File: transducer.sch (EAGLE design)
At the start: 12 parts, among them U1 ADS1014IDGST

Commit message: Transducer board routed.
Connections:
- net N$3 renamed ADR
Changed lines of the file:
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@@
 </segment>
 </net>
-<net name="N$3" class="0">
+<net name="ADR" class="0">
 <segment>
 <pinref part="U1" gate="A" pin="ADDR"/>

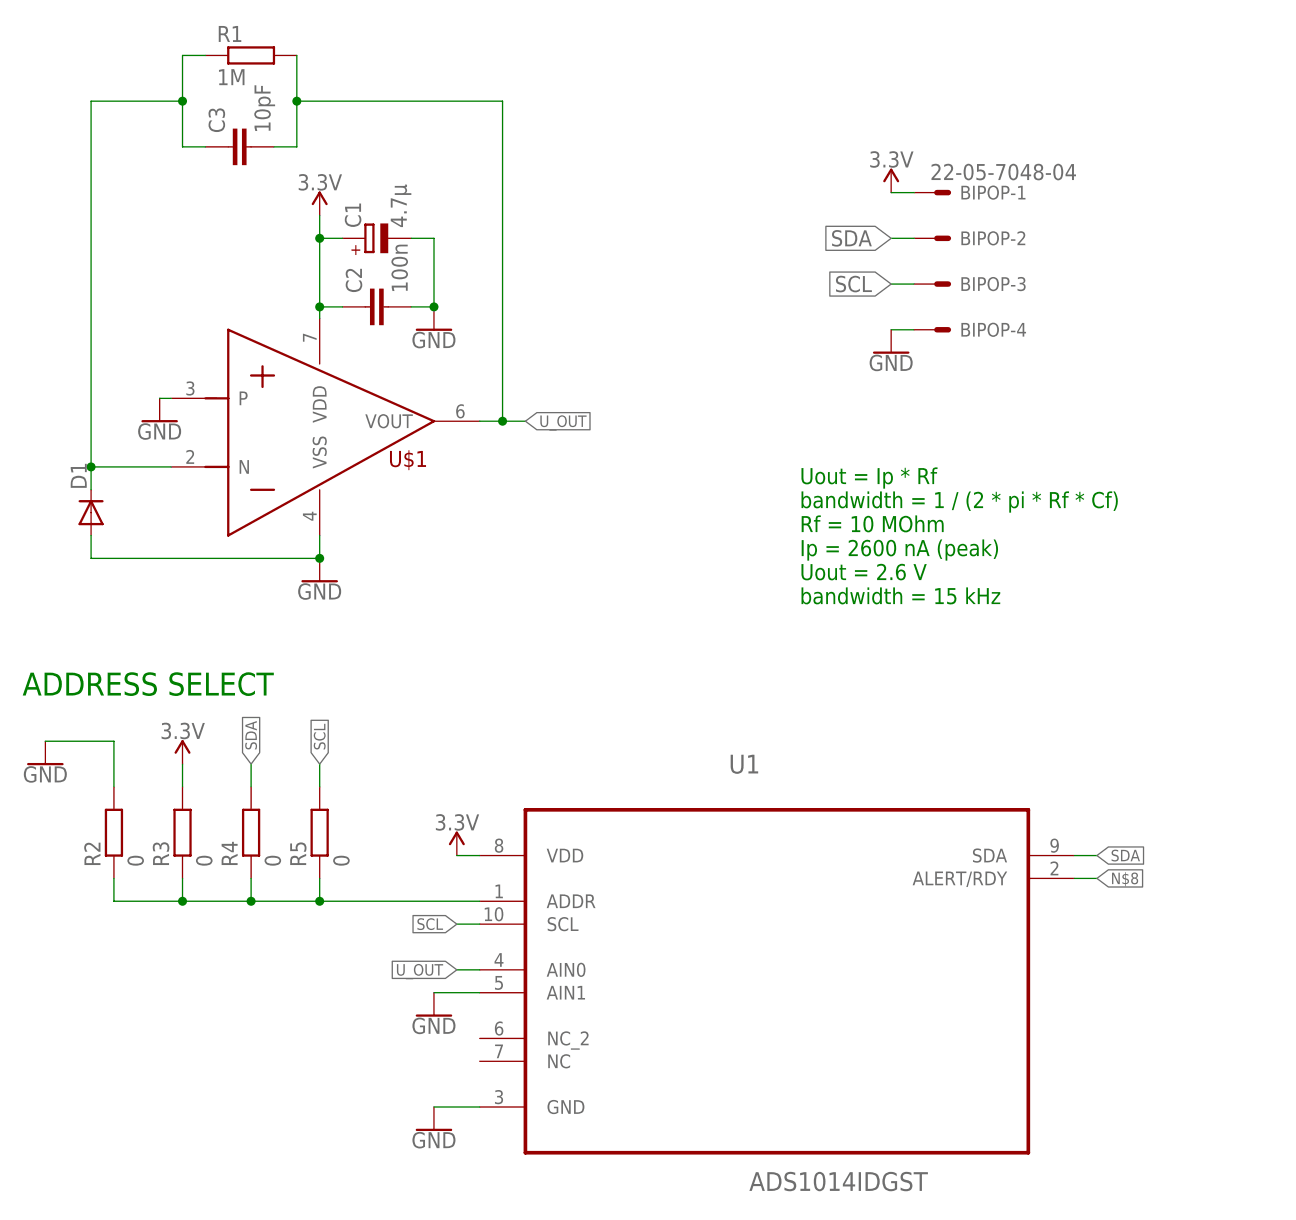
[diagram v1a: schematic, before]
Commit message: UV transducer board redesigned according to SGlux tips
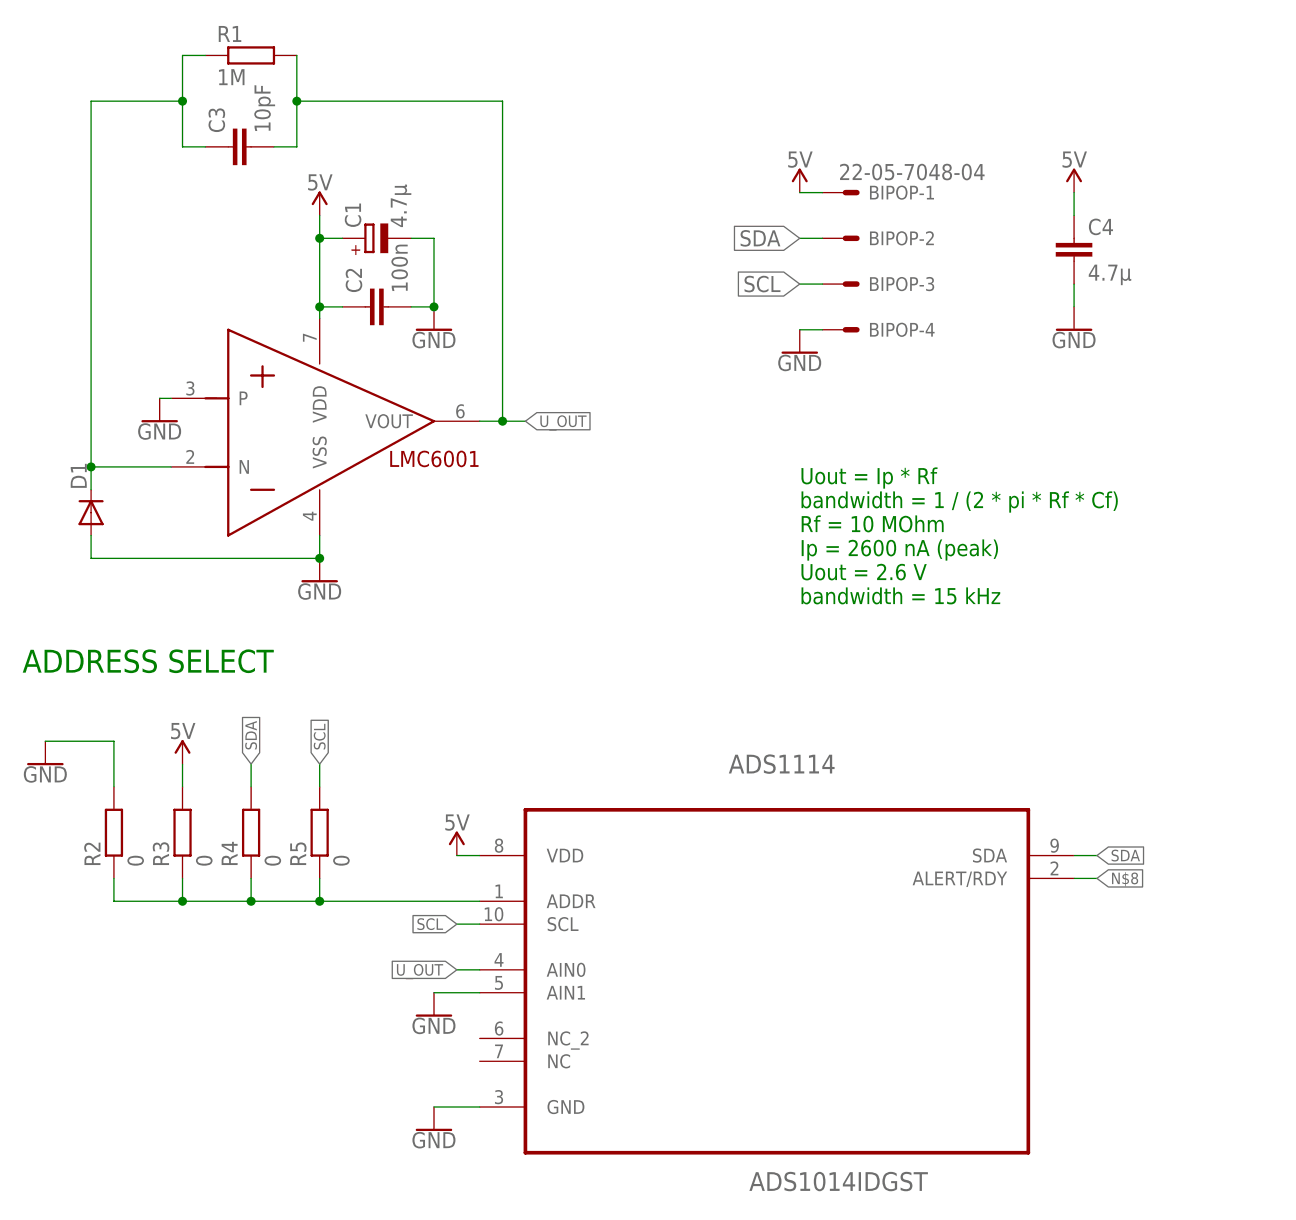
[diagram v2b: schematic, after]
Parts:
- added C4: 4.7µ, rcl:C-EUC0805
- renumbered U$1 to LMC6001, U1 to ADS1114
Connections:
- net N$5 renamed CATH
- removed net 3.3V: ADS1114.VDD, BIPOP-1.S, C1.+, C2.1, LMC6001.VDD, R3.2
- new net 5V: ADS1114.VDD, BIPOP-1.S, C1.+, C2.1, C4.1, LMC6001.VDD, R3.2
- net GND: now also C4.2
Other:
- moved on the sheet: BIPOP-1, BIPOP-2, BIPOP-3, BIPOP-4

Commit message: Transducer power supply and routing  modified.
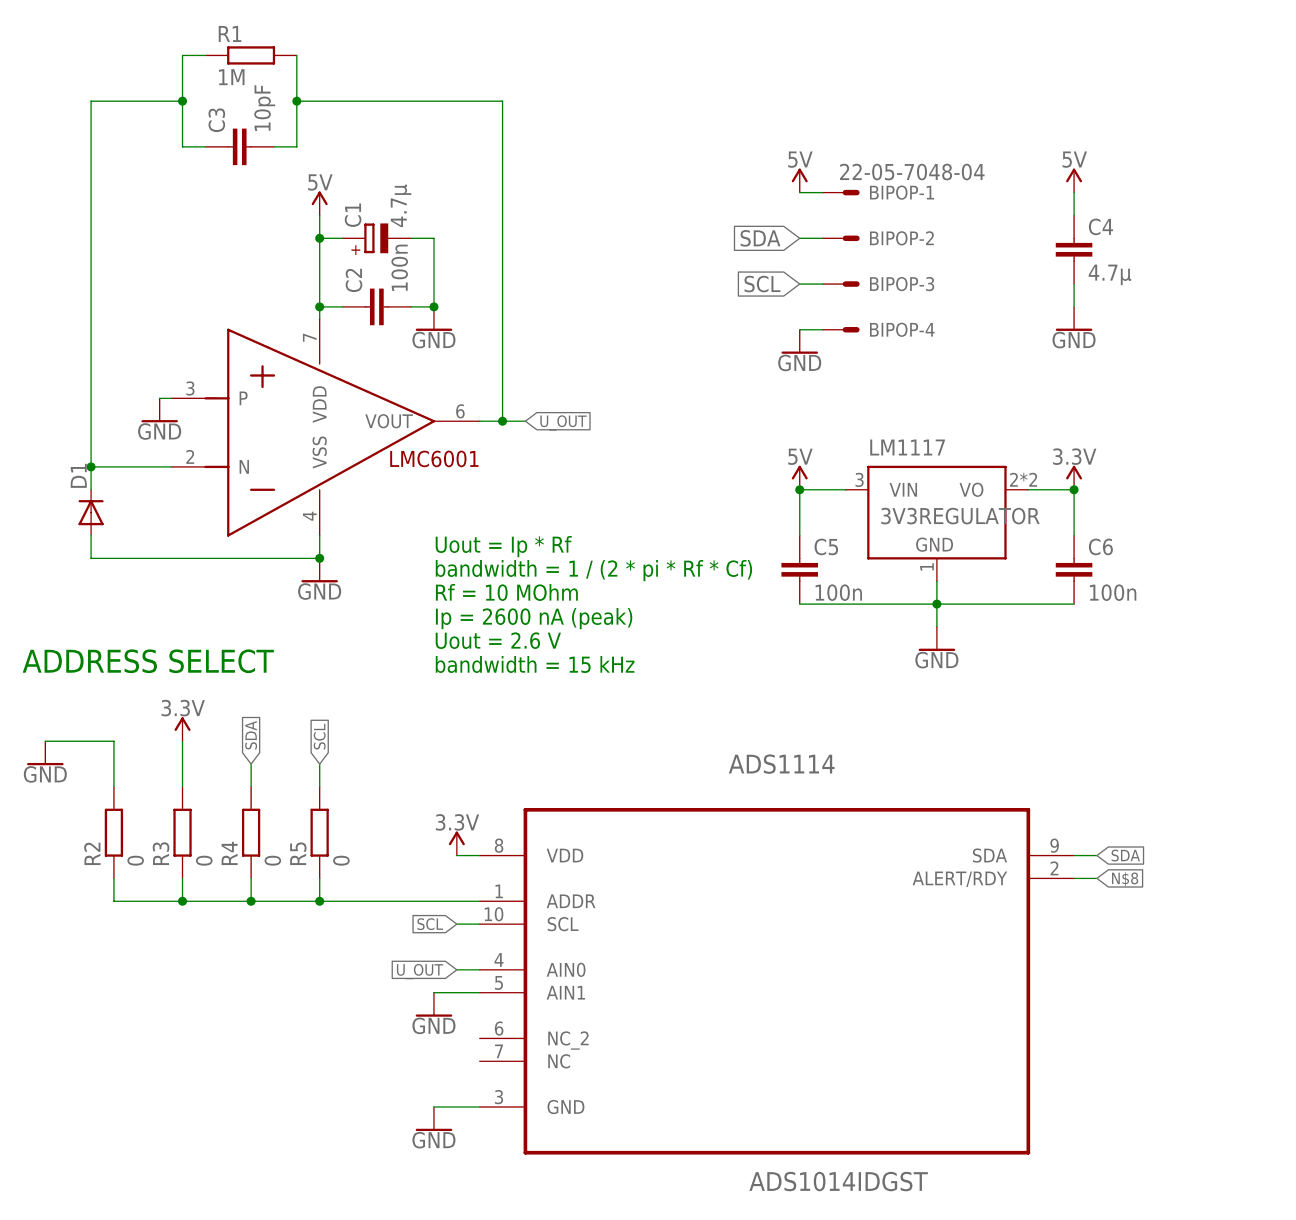
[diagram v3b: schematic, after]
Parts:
- added C5, C6: 100n, resistor:C-EUC0805
- added LM1117: 3V3REGULATOR, 3v3lm1117:3V3REGULATOR
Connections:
- new net 3.3V: ADS1114.VDD, C6.1, LM1117.VO, R3.2
- net 5V: now also C5.1, LM1117.VIN; no longer ADS1114.VDD, R3.2
- net GND: now also C5.2, C6.2, LM1117.GND
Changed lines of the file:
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@@
 <part name="C3" library="rcl" library_urn="urn:adsk.eagle:library:334" deviceset="C-EU" device="C0603" package3d_urn="urn:adsk.eagle:package:23616/2" value="10pF"/>
 <part name="ADS1114" library="Texas Instruments_By_element14_Batch_1" deviceset="ADS1014IDGST" device=""/>
-<part name="SUPPLY3" library="SparkFun-PowerSymbols" library_urn="urn:adsk.eagle:library:530" deviceset="5V" device=""/>
 <part name="GND4" library="SparkFun-PowerSymbols" library_urn="urn:adsk.eagle:library:530" deviceset="GND" device=""/>
 <part name="GND5" library="SparkFun-PowerSymbols" library_urn="urn:adsk.eagle:library:530" deviceset="GND" device=""/>
-<part name="SUPPLY4" library="SparkFun-PowerSymbols" library_urn="urn:adsk.eagle:library:530" deviceset="5V" device=""/>
 <part name="GND6" library="SparkFun-PowerSymbols" library_urn="urn:adsk.eagle:library:530" deviceset="GND" device=""/>
 <part name="R2" library="rcl" library_urn="urn:adsk.eagle:library:334" deviceset="R-EU_" device="R0805" package3d_urn="urn:adsk.eagle:package:23553/2" value="0"/>
@@
 <part name="GND10" library="SparkFun-PowerSymbols" library_urn="urn:adsk.eagle:library:530" deviceset="GND" device=""/>
 <part name="C4" library="rcl" library_urn="urn:adsk.eagle:library:334" deviceset="C-EU" device="C0805" package3d_urn="urn:adsk.eagle:package:23617/2" value="4.7µ"/>
+<part name="LM1117" library="3v3lm1117" deviceset="3V3REGULATOR" device=""/>
+<part name="GND8" library="SparkFun-PowerSymbols" library_urn="urn:adsk.eagle:library:530" deviceset="GND" device=""/>
+<part name="SUPPLY3" library="SparkFun-PowerSymbols" library_urn="urn:adsk.eagle:library:530" deviceset="5V" device=""/>
+<part name="SUPPLY4" library="SparkFun-PowerSymbols" library_urn="urn:adsk.eagle:library:530" deviceset="3.3V" device=""/>
+<part name="SUPPLY6" library="SparkFun-PowerSymbols" library_urn="urn:adsk.eagle:library:530" deviceset="3.3V" device=""/>
+<part name="SUPPLY7" library="SparkFun-PowerSymbols" library_urn="urn:adsk.eagle:library:530" deviceset="3.3V" device=""/>
+<part name="C5" library="resistor" library_urn="urn:adsk.eagle:library:348" deviceset="C-EU" device="C0805" package3d_urn="urn:adsk.eagle:package:26137/1" value="100n"/>
+<part name="C6" library="resistor" library_urn="urn:adsk.eagle:library:348" deviceset="C-EU" device="C0805" package3d_urn="urn:adsk.eagle:package:26137/1" value="100n"/>
 </parts>
 <sheets>
 <sheet>
 <plain>
-<text x="109.22" y="30.48" size="1.778" layer="91">Uout = Ip * Rf
+<text x="68.58" y="22.86" size="1.778" layer="91">Uout = Ip * Rf
 bandwidth = 1 / (2 * pi * Rf * Cf)
 Rf = 10 MOhm
@@
 <instance part="C3" gate="G$1" x="45.72" y="81.28" rot="R90"/>
 <instance part="ADS1114" gate="A" x="106.68" y="-7.62"/>
-<instance part="SUPPLY3" gate="G$1" x="71.12" y="2.54"/>
 <instance part="GND4" gate="1" x="68.58" y="-27.94"/>
 <instance part="GND5" gate="1" x="68.58" y="-15.24"/>
-<instance part="SUPPLY4" gate="G$1" x="40.64" y="12.7"/>
 <instance part="GND6" gate="1" x="25.4" y="12.7"/>
 <instance part="R2" gate="G$1" x="33.02" y="5.08" rot="R90"/>
@@
 <instance part="GND10" gate="1" x="139.7" y="60.96"/>
 <instance part="C4" gate="G$1" x="139.7" y="71.12"/>
+<instance part="LM1117" gate="G$1" x="124.46" y="40.64"/>
+<instance part="GND8" gate="1" x="124.46" y="25.4"/>
+<instance part="SUPPLY3" gate="G$1" x="109.22" y="43.18"/>
+<instance part="SUPPLY4" gate="G$1" x="139.7" y="43.18"/>
+<instance part="SUPPLY6" gate="G$1" x="40.64" y="15.24"/>
+<instance part="SUPPLY7" gate="G$1" x="71.12" y="2.54"/>
+<instance part="C5" gate="G$1" x="109.22" y="35.56"/>
+<instance part="C6" gate="G$1" x="139.7" y="35.56"/>
 </instances>
 <busses>
@@
 <pinref part="GND10" gate="1" pin="GND"/>
 <wire x1="139.7" y1="66.04" x2="139.7" y2="63.5" width="0.1524" layer="91"/>
+</segment>
+<segment>
+<pinref part="LM1117" gate="G$1" pin="GND"/>
+<pinref part="GND8" gate="1" pin="GND"/>
+<wire x1="124.46" y1="27.94" x2="124.46" y2="30.48" width="0.1524" layer="91"/>
+<pinref part="C6" gate="G$1" pin="2"/>
+<wire x1="124.46" y1="30.48" x2="124.46" y2="33.02" width="0.1524" layer="91"/>
+<wire x1="139.7" y1="30.48" x2="124.46" y2="30.48" width="0.1524" layer="91"/>
+<junction x="124.46" y="30.48"/>
+<pinref part="C5" gate="G$1" pin="2"/>
+<wire x1="109.22" y1="30.48" x2="124.46" y2="30.48" width="0.1524" layer="91"/>
 </segment>
 </net>
@@
 </segment>
 <segment>
-<wire x1="40.64" y1="12.7" x2="40.64" y2="10.16" width="0.1524" layer="91"/>
-<pinref part="SUPPLY4" gate="G$1" pin="5V"/>
-<pinref part="R3" gate="G$1" pin="2"/>
-</segment>
-<segment>
 <pinref part="SUPPLY1" gate="G$1" pin="5V"/>
 <pinref part="LMC6001" gate="G$1" pin="VDD"/>
@@
 </segment>
 <segment>
+<pinref part="LM1117" gate="G$1" pin="VIN"/>
+<pinref part="SUPPLY3" gate="G$1" pin="5V"/>
+<wire x1="109.22" y1="43.18" x2="114.3" y2="43.18" width="0.1524" layer="91"/>
+<pinref part="C5" gate="G$1" pin="1"/>
+<wire x1="109.22" y1="43.18" x2="109.22" y2="38.1" width="0.1524" layer="91"/>
+<junction x="109.22" y="43.18"/>
+</segment>
+</net>
+<net name="3.3V" class="0">
+<segment>
+<pinref part="LM1117" gate="G$1" pin="VO"/>
+<pinref part="SUPPLY4" gate="G$1" pin="3.3V"/>
+<wire x1="139.7" y1="43.18" x2="134.62" y2="43.18" width="0.1524" layer="91"/>
+<pinref part="C6" gate="G$1" pin="1"/>
+<wire x1="139.7" y1="43.18" x2="139.7" y2="38.1" width="0.1524" layer="91"/>
+<junction x="139.7" y="43.18"/>
+</segment>
+<segment>
+<pinref part="R3" gate="G$1" pin="2"/>
+<pinref part="SUPPLY6" gate="G$1" pin="3.3V"/>
+<wire x1="40.64" y1="15.24" x2="40.64" y2="10.16" width="0.1524" layer="91"/>
+</segment>
+<segment>
 <pinref part="ADS1114" gate="A" pin="VDD"/>
 <wire x1="73.66" y1="2.54" x2="71.12" y2="2.54" width="0.1524" layer="91"/>
-<pinref part="SUPPLY3" gate="G$1" pin="5V"/>
-</segment>
-</net>
+<pinref part="SUPPLY7" gate="G$1" pin="3.3V"/>
+</segment>
+</net>
